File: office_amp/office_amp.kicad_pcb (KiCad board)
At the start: 4 copper layers, 120 x 100 mm, 140 parts, among them J1 Jack-DC, J2 Conn_01x03_Female, J3 Conn_02x07_Odd_Even, J7 Screw_Terminal_01x04, J8 Conn_01x03_Female, K1 EC2-24NU, K2 EC2-24NU, K3 EC2-24NU, K4 EC2-24NU, Q1 DMT6012LSS, Q2 BC858, Q3 BC858, Q4 BC850, Q5 BC850, Q6 BC856, Q7 BC850, Q8 BC856, Q9 BC856, U1 LM74700, U10 DS1882E, U12 TL082, U2 TBA_2-2421, U3 TL082, U4 TBA_2-2421, U5 MH-M18, U6 TPA3123D2, U7 TL082, U8 IL300, U9 IL300

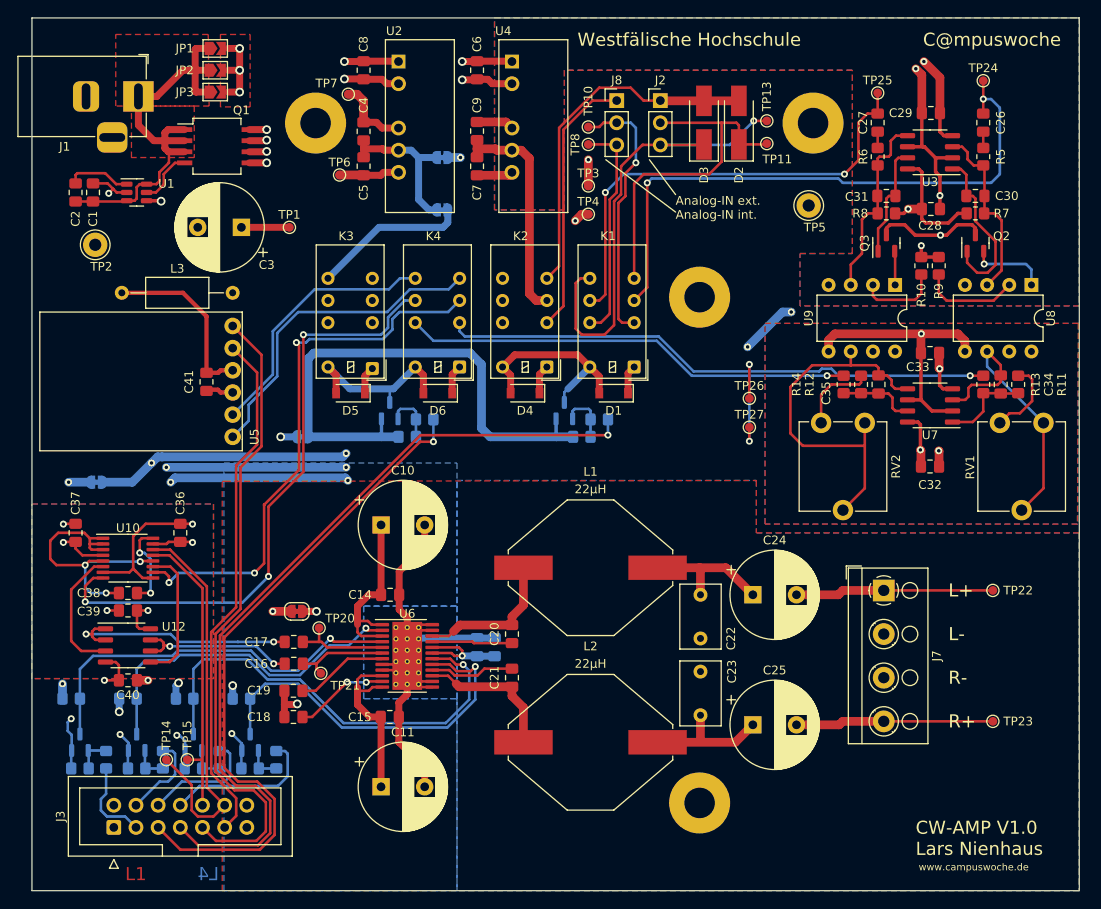
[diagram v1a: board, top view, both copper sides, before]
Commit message: First layout touch interface
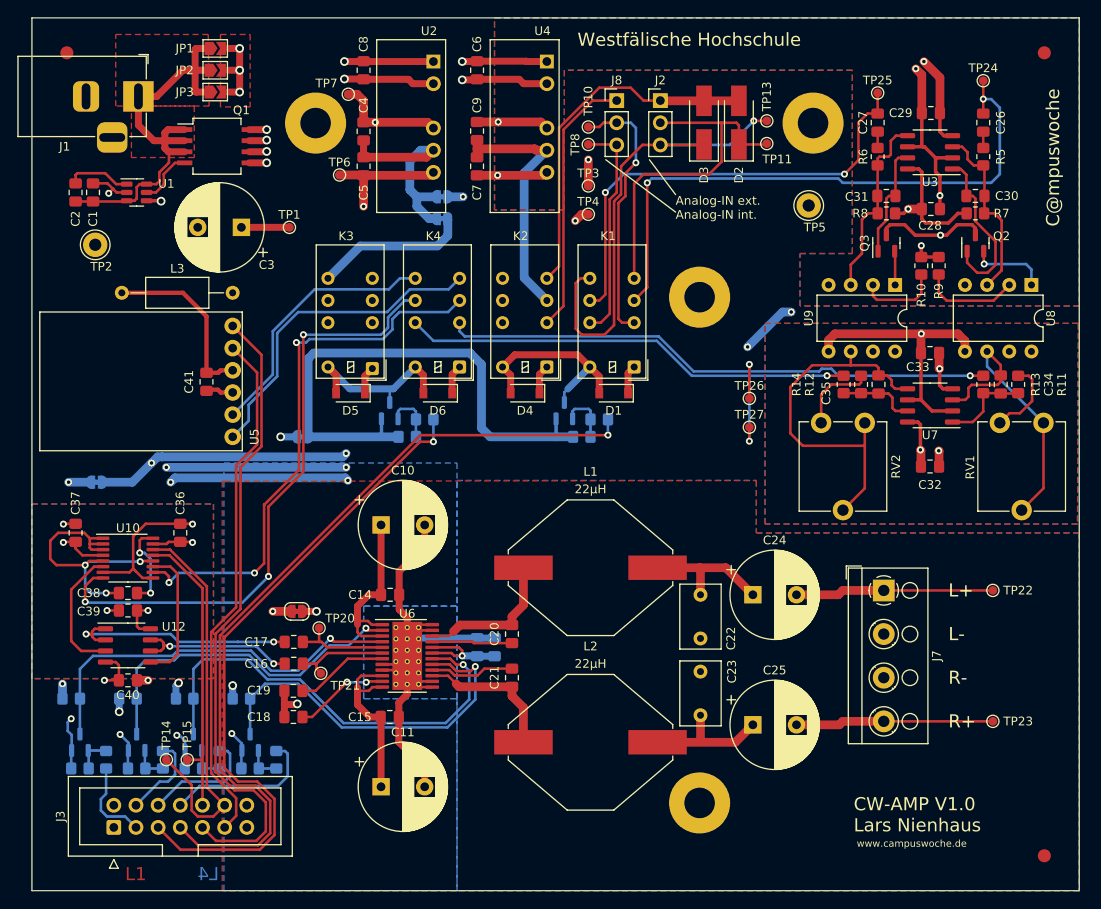
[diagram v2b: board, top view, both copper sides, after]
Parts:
- added FID1: Fiducial, Fiducial:Fiducial_1.5mm_Mask3mm, F.Cu at (94.0, 62.0)
- added FID2: Fiducial, Fiducial:Fiducial_1.5mm_Mask3mm, F.Cu at (206.0, 62.0)
- added FID3: Fiducial, Fiducial:Fiducial_1.5mm_Mask3mm, F.Cu at (206.0, 154.0)
- U2, U4: footprint MyLib:SIP-7 -> office_amp:SIP-7
- moved STAR4 4.50 mm to (137.0, 78.5)
- moved U2 4.00 mm to (136.0, 63.0)
- moved U4 4.00 mm to (149.0, 63.0)
- moved STAR2 1.00 mm to (137.0, 81.0)
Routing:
- net +5VA: track 106.7 -> 116.1 mm, vias 3 -> 4
- net GNDREF: track 369.2 -> 378.1 mm
- net V+: track 374.2 -> 382.7 mm
- net -5V: track 227.8 -> 234.9 mm, vias 7 -> 8
- net Net-(C4-Pad1): track 18.0 -> 24.1 mm
- net +5V: track 262.6 -> 268.4 mm, vias 5 -> 6
- net GNDA: track 290.7 -> 287.6 mm
- net GND_Input: track 154.3 -> 155.1 mm
- net -5VA: track 89.4 -> 89.3 mm, vias 2 -> 3

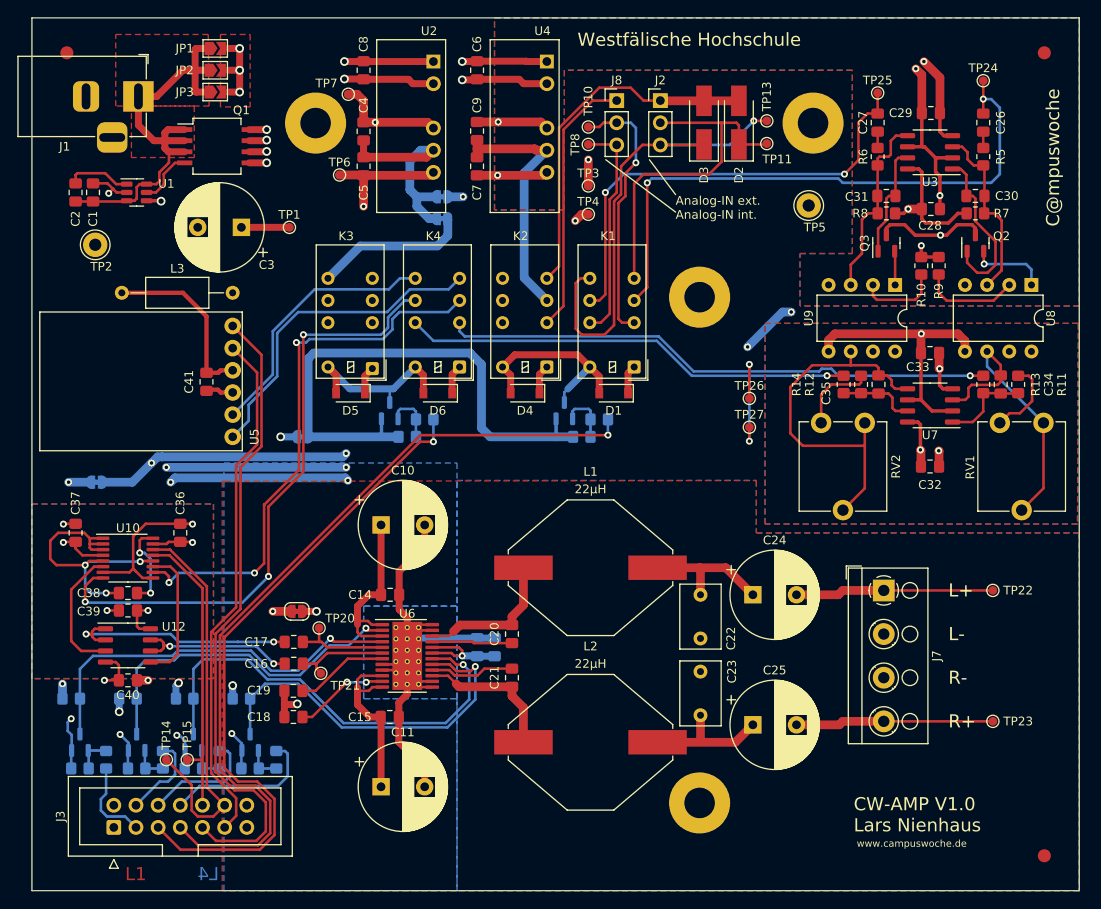
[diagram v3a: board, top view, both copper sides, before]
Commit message: Added CHanges from Testing, first layout V1.5
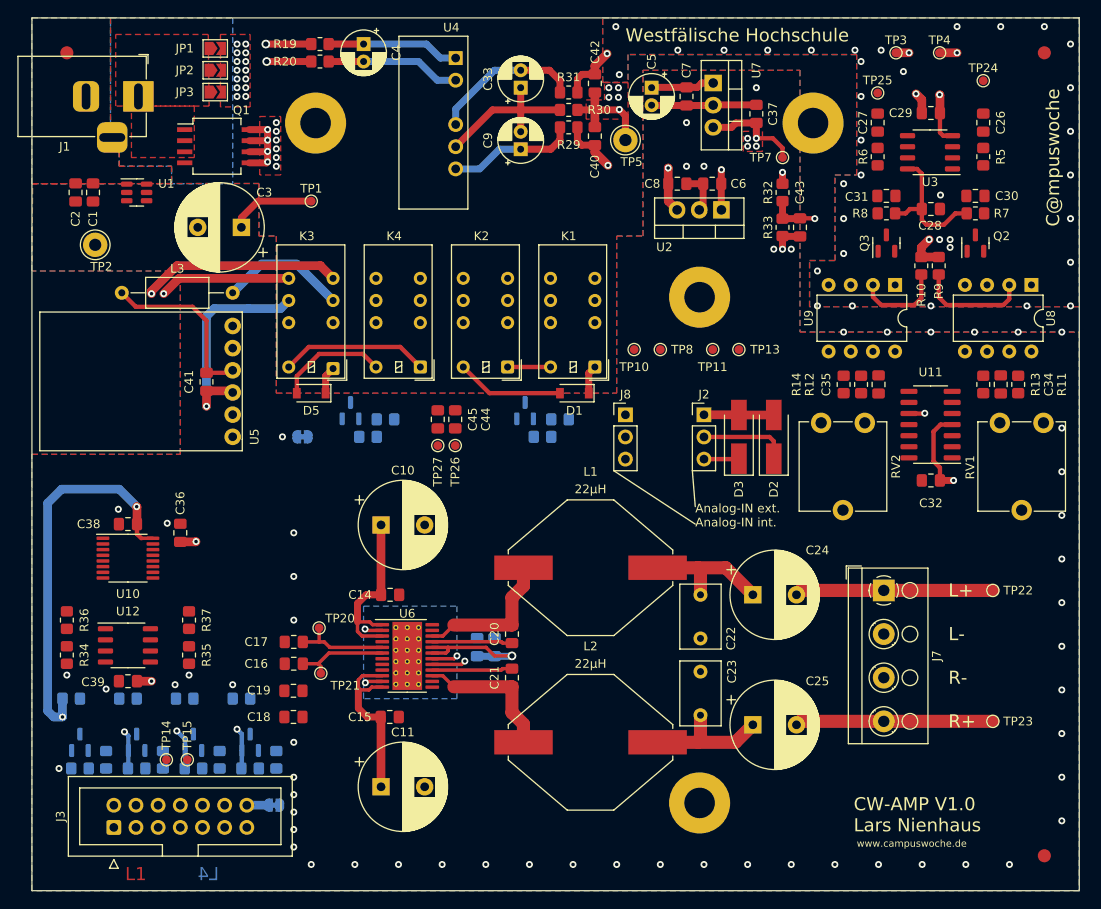
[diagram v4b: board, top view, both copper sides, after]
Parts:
- removed D4, D6: 1N4148W, Diode_SMD:D_SOD-123
- removed STAR1, STAR2, STAR4: SolderJumper_2_Bridged, Jumper:SolderJumper-2_P1.3mm_Bridged_RoundedPad1.0x1.5mm
- removed TP6: TestPoint, TestPoint:TestPoint_Pad_D1.0mm
- added C42: 100nF, Capacitor_SMD:C_0805_2012Metric_Pad1.18x1.45mm_HandSolder, F.Cu at (154.5, 65.5)
- added C43: 2µ2F, Capacitor_SMD:C_0805_2012Metric_Pad1.18x1.45mm_HandSolder, F.Cu at (178.0, 82.0)
- added C44: 2µ2F, Capacitor_SMD:C_0805_2012Metric_Pad1.18x1.45mm_HandSolder, F.Cu at (138.5, 104.0)
- added C45: 2µ2F, Capacitor_SMD:C_0805_2012Metric_Pad1.18x1.45mm_HandSolder, F.Cu at (136.5, 104.0)
- added R19: 10R, Resistor_SMD:R_0805_2012Metric_Pad1.20x1.40mm_HandSolder, F.Cu at (123.0, 61.0)
- added R20: 10R, Resistor_SMD:R_0805_2012Metric_Pad1.20x1.40mm_HandSolder, F.Cu at (123.0, 63.0)
- added R29: 0R, Resistor_SMD:R_0805_2012Metric_Pad1.20x1.40mm_HandSolder, F.Cu at (151.5, 70.5)
- added R30: 0R, Resistor_SMD:R_0805_2012Metric_Pad1.20x1.40mm_HandSolder, F.Cu at (151.5, 68.5)
- added R31: 0R, Resistor_SMD:R_0805_2012Metric_Pad1.20x1.40mm_HandSolder, F.Cu at (151.5, 66.5)
- added R32: 10k, Resistor_SMD:R_0805_2012Metric_Pad1.20x1.40mm_HandSolder, F.Cu at (176.0, 78.0)
- added R33: 10k, Resistor_SMD:R_0805_2012Metric_Pad1.20x1.40mm_HandSolder, F.Cu at (176.0, 82.0)
- added R34: 10k, Resistor_SMD:R_0805_2012Metric_Pad1.20x1.40mm_HandSolder, F.Cu at (94.0, 131.0)
- added R35: 10k, Resistor_SMD:R_0805_2012Metric_Pad1.20x1.40mm_HandSolder, F.Cu at (108.0, 131.0)
- added R36: ?, Resistor_SMD:R_0805_2012Metric_Pad1.20x1.40mm_HandSolder, F.Cu at (94.0, 127.0)
- added R37: ?, Resistor_SMD:R_0805_2012Metric_Pad1.20x1.40mm_HandSolder, F.Cu at (108.0, 127.0)
- added U11: TL084, Package_SO:SOIC-14_3.9x8.7mm_P1.27mm, F.Cu at (193.0, 104.6)
- C33: value 100nF -> 4,7µF; footprint Capacitor_SMD:C_0805_2012Metric_Pad1.18x1.45mm_HandSolder -> Capacitor_THT:CP_Radial_D5.0mm_P2.00mm
- C4, C5, C9: value 10µF -> 4,7µF; footprint Capacitor_SMD:C_0805_2012Metric_Pad1.18x1.45mm_HandSolder -> Capacitor_THT:CP_Radial_D5.0mm_P2.00mm
- C6, C7, C8: value 10µF -> 100nF
- K1, K2, K3, K4: value EC2-24NU -> V23079-A1003-B301
- U2: value TBA_2-2421 -> LM7805_TO220; footprint office_amp:SIP-7 -> Package_TO_SOT_THT:TO-220-3_Vertical
- U7: value TL082 -> LM7812_TO220; footprint Package_SO:SO-8_3.9x4.9mm_P1.27mm -> Package_TO_SOT_THT:TO-220-3_Vertical
- moved C37 91.6 mm to (173.0, 69.0), turned to 90 degrees
- moved C40 82.2 mm to (154.5, 71.5), turned to 90 degrees
- moved C33 55.9 mm to (146.0, 66.0), turned to 90 degrees
- moved TP7 50.3 mm to (176.0, 74.0)
- moved U7 44.5 mm to (168.1, 65.5), turned to -90 degrees
- moved TP4 44.3 mm to (194.0, 62.0)
- moved STAR3 42.2 mm to (117.8, 148.2)
- moved TP3 38.4 mm to (189.0, 62.0)
- moved C8 38.2 mm to (163.9, 77.0), turned to 0 degrees
- moved U2 37.1 mm to (169.0, 80.0), turned to 180 degrees
- moved J2 36.3 mm to (167.0, 103.5)
- moved D2 36.2 mm to (175.0, 106.0)
- moved D3 36.2 mm to (171.0, 106.0)
- moved J8 36.0 mm to (158.0, 103.5)
- moved TP27 35.8 mm to (136.5, 107.0), turned to -90 degrees
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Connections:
- C32 pad 1: +5V -> +12V
- C32 pad 2: GNDA -> GNDREF
- C33 pad 1: GNDA -> Net-(U4-Pad5)
- C33 pad 2: -5V -> Net-(U4-Pad4)
- C36 pad 2: GNDA -> GNDREF
- C37 pad 1: GNDA -> +12V
- C37 pad 2: -5V -> GNDREF
- C38 pad 2: GNDD -> GNDREF
- C39 pad 2: GNDA -> GNDREF
- C4 pad 1: Net-(C4-Pad1) -> Net-(U4-Pad1)
- C4 pad 2: -5V -> Net-(U4-Pad2)
- C40 pad 1: GNDA -> +5VA
- C40 pad 2: -5V -> GND_Input
- C5 pad 1: +5V -> V+
- C5 pad 2: Net-(C4-Pad1) -> GNDREF
- C6 pad 1: V+ -> +12V
- C7 pad 1: +5VA -> V+
- C7 pad 2: GND_Input -> GNDREF
- C8 pad 1: V+ -> +5V
- C9 pad 1: GND_Input -> Net-(U4-Pad6)
- C9 pad 2: -5VA -> Net-(U4-Pad5)
- D1 pad 2: Net-(D1-Pad2) -> Net-(Q4-Pad3)
- D5 pad 2: Net-(D5-Pad2) -> Net-(K4-Pad12)
- K1 pad 12: Net-(D1-Pad2) -> Net-(K1-Pad12)
- K2 pad 1: V+ -> Net-(K1-Pad12)
- K2 pad 12: Net-(D1-Pad2) -> Net-(Q4-Pad3)
- K3 pad 12: Net-(D5-Pad2) -> Net-(K4-Pad1)
- K3 pad 8: GND1 -> GNDD
- K4 pad 1: V+ -> Net-(K4-Pad1)
- K4 pad 12: Net-(D5-Pad2) -> Net-(K4-Pad12)
- Q4 pad 3: Net-(D1-Pad2) -> Net-(Q4-Pad3)
- Q5 pad 3: Net-(D5-Pad2) -> Net-(K4-Pad12)
- R13 pad 1: R-In-OPA -> Net-(R13-Pad1)
- R14 pad 1: L-In-OPA -> Net-(R14-Pad1)
- STAR3 pad 2: GNDA -> GNDREF
- TP26 pad 1: R-In-OPA -> Net-(R13-Pad1)
- TP27 pad 1: L-In-OPA -> Net-(R14-Pad1)
- TP7 pad 1: -5V -> +12V
- U10 pad 1: GNDD -> GNDREF
- U10 pad 12: GNDD -> GNDREF
- U10 pad 2: GNDD -> GNDREF
- U10 pad 3: GNDD -> GNDREF
- U10 pad 4: -5V -> GNDREF
- U10 pad 5: GNDD -> GNDREF
- U10 pad 7: GNDA -> GNDREF
- U10 pad 9: GNDA -> GNDREF
- U12 pad 2: Net-(C17-Pad2) -> Net-(U12-Pad2)
- U12 pad 4: -5V -> GNDREF
- U12 pad 6: Net-(C16-Pad2) -> Net-(U12-Pad6)
- U2 pad 1: V+ -> +12V
- U3 pad 2: GND_Input -> Net-(C30-Pad2)
- U3 pad 3: Net-(C30-Pad2) -> GND_Input
- U3 pad 5: Net-(C31-Pad2) -> GND_Input
- U3 pad 6: GND_Input -> Net-(C31-Pad2)
- U4 pad 1: V+ -> Net-(U4-Pad1)
- U4 pad 2: GNDREF -> Net-(U4-Pad2)
- U4 pad 4: -5VA -> Net-(U4-Pad4)
- U4 pad 5: GND_Input -> Net-(U4-Pad5)
- U4 pad 6: +5VA -> Net-(U4-Pad6)
- U7 pad 1: Net-(C34-Pad1) -> V+
- U7 pad 2: GNDA -> GNDREF
- U7 pad 3: Net-(C34-Pad2) -> +12V
- U8 pad 5: GNDA -> Net-(U8-Pad5)
- U9 pad 5: GNDA -> Net-(U8-Pad5)
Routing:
- net GNDA: track 287.6 -> 0.00 mm, vias 10 -> 0
- net -5V: track 234.9 -> 0.00 mm, vias 8 -> 0
- net GNDREF: track 378.1 -> 188.6 mm, vias 10 -> 59
- net SELECT-Analog: track 93.8 -> 0.00 mm, vias 1 -> 0
- net +5V: track 268.4 -> 361.7 mm, vias 6 -> 4
- net +12V: track 0.00 -> 84.7 mm, vias 0 -> 7
- net GND_Input: track 155.1 -> 75.6 mm, vias 3 -> 41
- net SELECT-BT: track 77.2 -> 0.00 mm, vias 1 -> 0
- net BT-KEY: track 73.5 -> 0.00 mm
- net L-In: track 71.0 -> 0.00 mm, vias 3 -> 0
- net R-In-ISO: track 69.0 -> 0.00 mm, vias 2 -> 0
- net R-In-OPA: track 68.0 -> 0.00 mm, vias 2 -> 0
- net V+: track 382.7 -> 318.2 mm, vias 11 -> 26
- net R-In: track 63.0 -> 0.00 mm, vias 3 -> 0
- net GND2: track 62.3 -> 0.00 mm
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- added copper zone on F.Cu, net +12V
- removed copper zone on B.Cu, net GNDA
- removed copper zone on F.Cu, net GNDA
- removed copper zone on In1.Cu, net GNDA

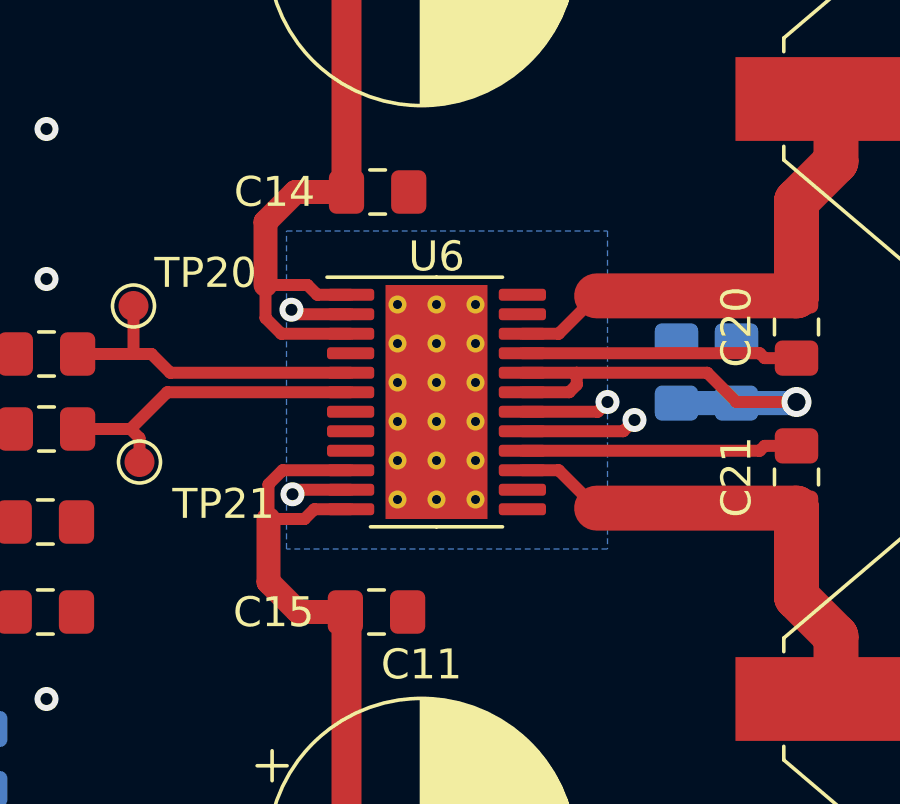
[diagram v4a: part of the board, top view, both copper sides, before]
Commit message: Organized Schematic
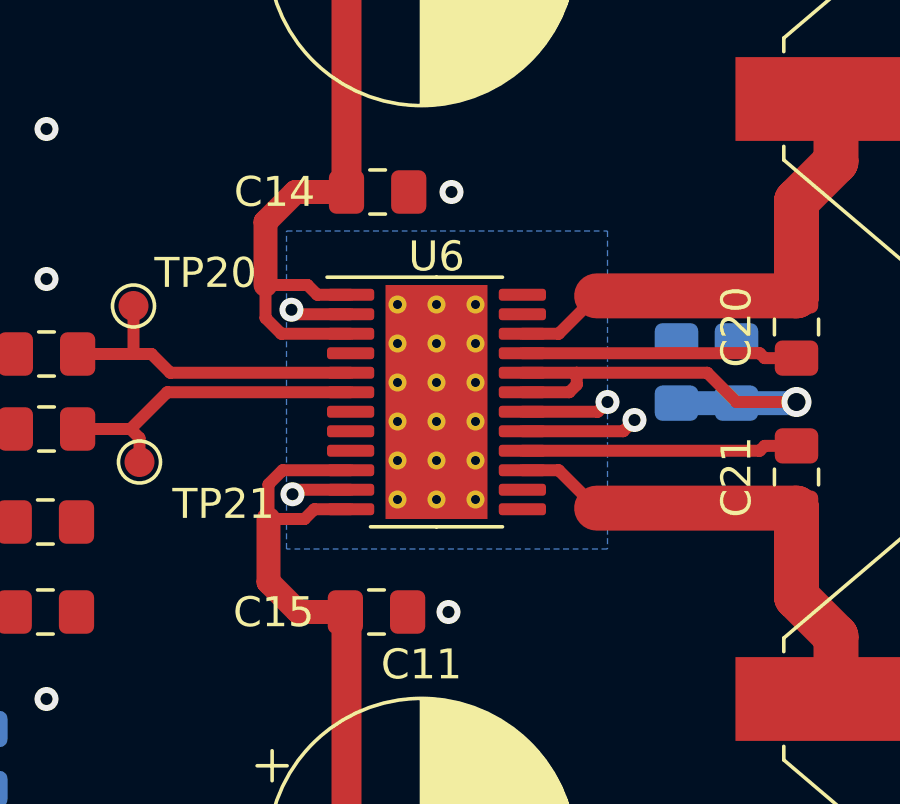
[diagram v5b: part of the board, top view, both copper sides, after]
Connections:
- net AMP-GAIN0 renamed /Class_D/AMP-GAIN0
- net AMP-GAIN1 renamed /Class_D/AMP-GAIN1
- net AMP-ShutDown renamed /Class_D/AMP-ShutDown
- net ANALOG-BIAS renamed /Audio_Isolation/ANALOG-BIAS
- net L-In renamed /Class_D/L-In
- net L-In-ISO renamed /Audio_Isolation/L-In-ISO
- net L-In-OPA renamed /Audio_Isolation/L-In-OPA
- net R-In renamed /Class_D/R-In
- net R-In-ISO renamed /Audio_Isolation/R-In-ISO
- net R-In-OPA renamed /Audio_Isolation/R-In-OPA
- net SCL renamed /Class_D/SCL
- net SDA renamed /Class_D/SDA
- net ~{AMP-Mute} renamed /Class_D/~{AMP-Mute}
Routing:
- net GNDREF: vias 59 -> 61
